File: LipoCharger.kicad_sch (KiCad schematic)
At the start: 34 parts, among them J1 S2B-XH-A, J2 USB_C_Receptacle_USB2.0_14P, Q1 SI2300A, Q2 SI2300A, Q3 HL 2305A, SW1 SK12D07VG4, U1 TP4056-42-ESOP8, U2 MT3608, U3 FM2113

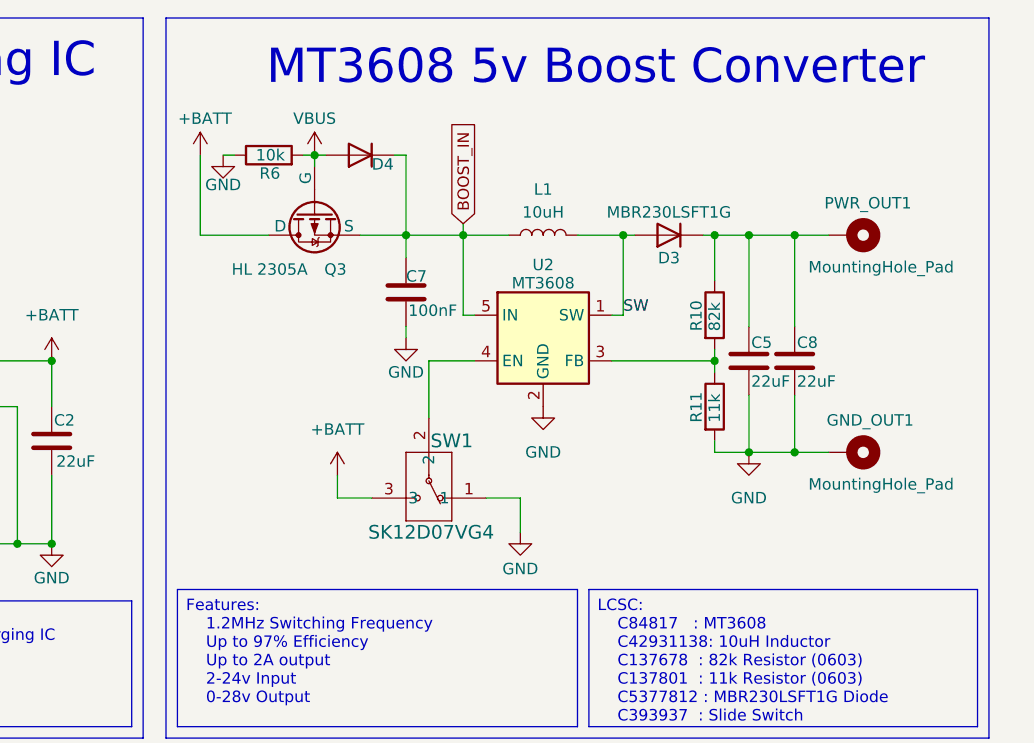
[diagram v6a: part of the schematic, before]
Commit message: Fixed issue that would allow power to flow even thought the power switch is turned off
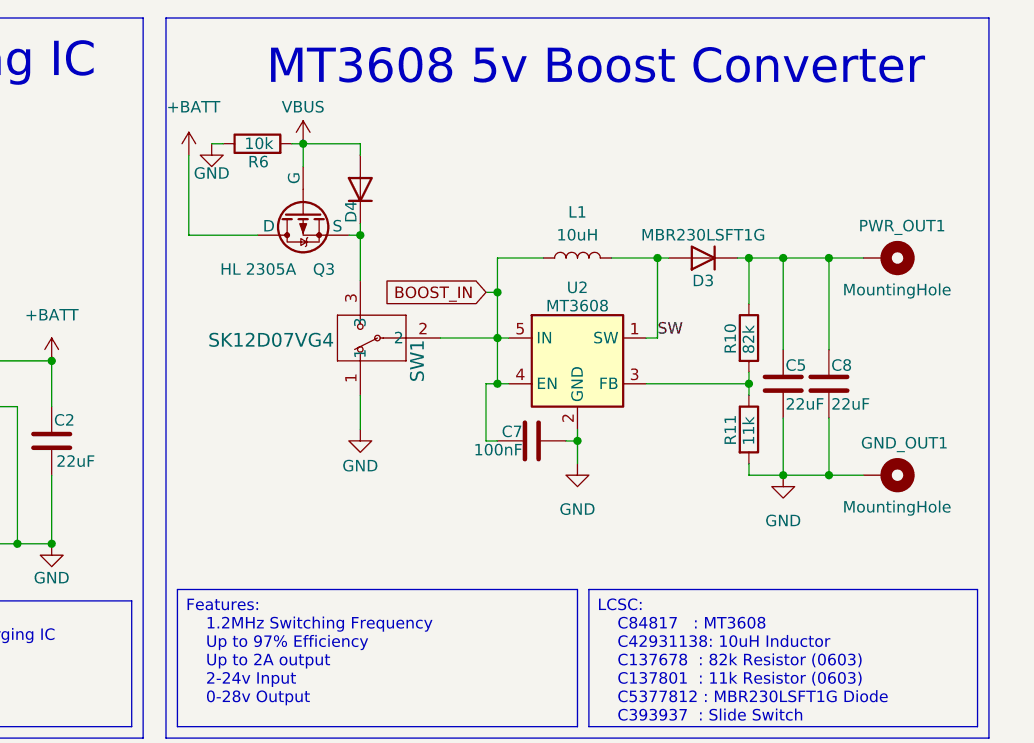
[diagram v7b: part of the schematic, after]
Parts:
- GND_OUT1, PWR_OUT1: value MountingHole_Pad -> MountingHole
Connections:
- net +BATT: no longer SW1.3
- net BOOST_IN: now also SW1.2, U2.4 (EN); no longer D4.1 (K), Q3.2 (S)
- new net: D4.1 (K), Q3.2 (S), SW1.3
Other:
- moved on the sheet: C5, C7, C8, D3, D4, GND_OUT1, L1, PWR_OUT1, Q3, R10, R11, R6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
